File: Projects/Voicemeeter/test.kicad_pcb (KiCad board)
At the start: 2 copper layers, 348.5 x 271.7 mm, 226 parts, among them J501 CONN_01X05, J502 CONN_01X03, J503 CONN_01X05, J504 CONN_01X02, J505 CONN_01X03, J506 CONN_01X02, J509 Screw_Terminal_1x02, SW201 SW_SPDT_6pin, SW202 SW_SPDT_6pin, SW203 SW_SPDT_6pin, SW204 SW_SPDT_6pin, SW205 SW_SPDT_6pin, SW206 SW_SPDT_6pin, SW207 SW_SPDT_6pin, SW208 SW_SPDT_6pin, SW209 SW_SPDT_6pin, SW210 SW_SPDT_6pin, SW211 SW_SPDT_6pin, SW212 SW_SPDT_6pin, SW213 SW_SPDT_6pin, SW214 SW_SPDT_6pin, SW215 SW_SPDT_6pin, SW216 SW_SPDT_6pin, SW217 SW_SPDT_6pin, SW218 SW_SPDT_6pin, SW219 SW_SPDT_6pin, SW220 SW_SPDT_6pin, SW221 SW_SPDT_6pin, SW222 SW_SPDT_6pin, SW223 SW_SPDT_6pin, SW224 SW_SPDT_6pin, SW225 SW_SPDT_6pin, SW226 SW_SPDT_6pin, SW227 SW_SPDT_6pin, SW228 SW_SPDT_6pin, SW229 SW_SPDT_6pin, SW230 SW_SPDT_6pin, SW231 SW_SPDT_6pin, SW232 SW_SPDT_6pin, SW233 SW_SPDT_6pin, SW234 SW_SPDT_6pin, SW235 SW_SPDT_6pin, SW236 SW_SPDT_6pin, SW237 SW_SPDT_6pin, SW238 SW_SPDT_6pin, SW239 SW_SPDT_6pin, SW240 SW_SPDT_6pin, SW241 SW_SPDT_6pin, SW242 SW_SPDT_6pin, SW243 SW_SPDT_6pin, SW244 SW_SPDT_6pin, SW245 SW_SPDT_6pin, SW246 SW_SPDT_6pin, SW247 SW_SPDT_6pin, SW248 SW_SPDT_6pin, SW249 SW_SPDT_6pin, SW250 SW_SPDT_6pin, SW251 SW_SPDT_6pin, SW252 SW_SPDT_6pin, SW253 SW_SPDT_6pin, SW254 SW_SPDT_6pin, SW255 SW_SPDT_6pin, SW501 SW_Push, U401 74HC4051, U402 74HC4051, U403 74HC4051, U404 74HC4051, U405 74HC4051, U406 74HC4051, U407 74HC4051, U408 74HC4051, U409 74HC4051, U410 74HC4051, U501 stm32f103-china-MS, U502 PC817

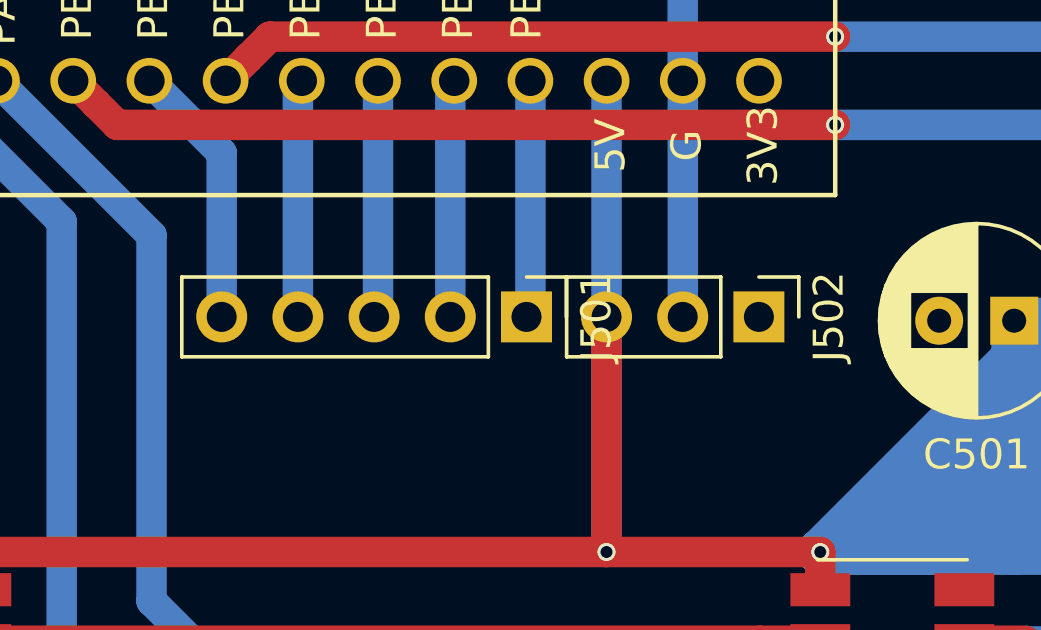
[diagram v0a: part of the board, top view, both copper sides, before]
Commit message: fixed a header
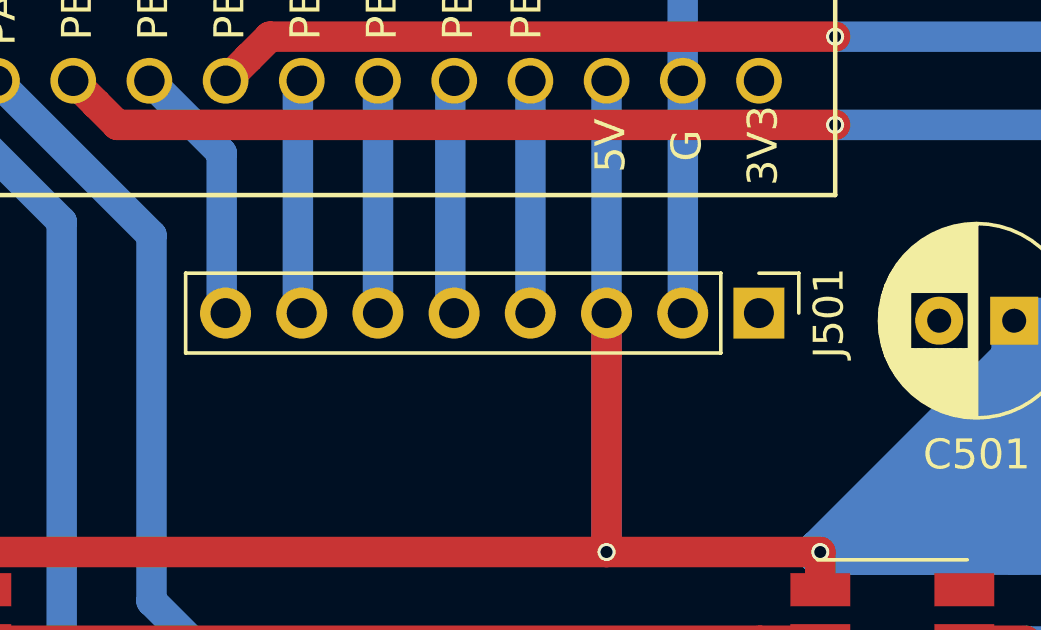
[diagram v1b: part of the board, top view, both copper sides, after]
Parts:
- removed J502: CONN_01X03, Pin_Headers:Pin_Header_Straight_1x03_Pitch2.54mm
- J501: value CONN_01X05 -> Conn_01x08; footprint Pin_Headers:Pin_Header_Straight_1x05_Pitch2.54mm -> Pin_Headers:Pin_Header_Straight_1x08_Pitch2.54mm
- moved J501 7.75 mm to (273.7, 108.0)
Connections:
- J501 pad 1: Net-(J501-Pad1) -> +3V3
- J501 pad 2: Net-(J501-Pad2) -> GND
- J501 pad 3: Net-(J501-Pad3) -> +5V
- U501 pad 12: Net-(J501-Pad5) -> Net-(J501-Pad8)
- U501 pad 14: Net-(J501-Pad4) -> Net-(J501-Pad7)
- U501 pad 15: Net-(J501-Pad3) -> Net-(J501-Pad6)
- U501 pad 16: Net-(J501-Pad2) -> Net-(J501-Pad5)
- U501 pad 17: Net-(J501-Pad1) -> Net-(J501-Pad4)
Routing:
- net Net-(J501-Pad8): track 0.00 -> 8.62 mm
- net Net-(J501-Pad7): track 0.00 -> 7.67 mm
- net Net-(J501-Pad3): track 7.67 -> 0.00 mm
- net Net-(J501-Pad2): track 7.67 -> 0.00 mm
- net Net-(J501-Pad1): track 7.67 -> 0.00 mm
- net Net-(J501-Pad6): track 0.00 -> 7.49 mm
- net Net-(J501-Pad5): track 8.62 -> 7.67 mm

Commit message: stuff
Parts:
- added C1, C10, C11, C12, C13, C14, C15, C16, C17, C18, C19, C2, C20, C21, C22, C3, C4, C5, C6, C7, C8, C9: 10uF, Capacitors_SMD:C_1206_HandSoldering, F.Cu at (206.8, 256.4)
- added C23, C24: 220uF, Capacitors_THT:CP_Radial_D6.3mm_P2.50mm, F.Cu at (206.8, 256.4)
- added D1: D, Diodes_THT:D_DO-41_SOD81_P12.70mm_Horizontal, F.Cu at (206.8, 256.4)
- added J1: SPARE, Pin_Headers:Pin_Header_Straight_1x05_Pitch2.54mm, F.Cu at (206.8, 256.4)
- added J2, J4: GS2, MATHSTERK:SB2, F.Cu at (206.8, 256.4)
- added J3: Screw_Terminal_01x02, Connectors_Terminal_Blocks:TerminalBlock_Altech_AK300-2_P5.00mm, F.Cu at (206.8, 256.4)
- added J5: MIDI OUT, Pin_Headers:Pin_Header_Straight_1x03_Pitch2.54mm, F.Cu at (206.8, 256.4)
- added J6: MIDI IN, Pin_Headers:Pin_Header_Straight_1x02_Pitch2.54mm, F.Cu at (206.8, 256.4)
- added LED1, LED10, LED11, LED12, LED13, LED14, LED15, LED16, LED17, LED18, LED19, LED2, LED20, LED21, LED22, LED23, LED24, LED25, LED26, LED27, LED28, LED29, LED3, LED30, LED31, LED32, LED4, LED5, LED6, LED7, LED8, LED9: SK9822, LEDs:LED_RGB_5050-6, F.Cu at (206.8, 256.4)
- added R1, R10, R11, R12, R13, R14, R15, R16, R17, R18, R19, R2, R20, R21, R22, R23, R24, R25, R26, R27, R28, R29, R3, R30, R31, R32, R33, R34, R35, R36, R37, R38, R39, R4, R40, R41, R42, R43, R44, R45, R46, R47, R48, R49, R5, R50, R51, R52, R53, R54, R55, R6, R7, R8, R9: 10K, Resistors_SMD:R_1206_HandSoldering, F.Cu at (206.8, 256.4)
- added R56, R57, R58, R59, R60, R61, R62, R63, R64, R65, R66, R67, R68, R70, R71, R72, R73, R75, R77: 10k, Resistors_SMD:R_1206_HandSoldering, F.Cu at (206.8, 256.4)
- added R69, R76: 220R, Resistors_SMD:R_1206_HandSoldering, F.Cu at (206.8, 256.4)
- added R74: 330R, Resistors_SMD:R_1206_HandSoldering, F.Cu at (206.8, 256.4)
- added RESET1: SW_Push, Buttons_Switches_THT:SW_PUSH-12mm, F.Cu at (206.8, 256.4)
- added RV1, RV11, RV12, RV13, RV15, RV16, RV17, RV3, RV4, RV6, RV7, RV9: POT, Potentiometers:Potentiometer_Omeg_PC16PU_Horizontal, F.Cu at (206.8, 256.4)
- added RV10, RV14, RV18, RV19, RV2, RV20, RV21, RV22, RV5, RV8: SLIDEPOT, MATHSTERK:slidepot, F.Cu at (206.8, 256.4)
- added SW1, SW10, SW11, SW12, SW13, SW14, SW15, SW16, SW17, SW18, SW19, SW2, SW20, SW21, SW22, SW23, SW24, SW25, SW26, SW27, SW28, SW29, SW3, SW30, SW31, SW32, SW33, SW34, SW35, SW36, SW37, SW38, SW39, SW4, SW40, SW41, SW42, SW43, SW44, SW45, SW46, SW47, SW48, SW49, SW5, SW50, SW51, SW52, SW53, SW54, SW55, SW6, SW7, SW8, SW9: SW_SPDT_6pin, MATHSTERK:8mm_push_button, F.Cu at (206.8, 256.4)
- added SW56: PEC11R-4215F-S0024, MATHSTERK:Rotary_Encoder_Switched_PEC11R, F.Cu at (206.8, 256.4)
- added U1, U10, U2, U3, U4, U5, U6, U7, U8, U9: 74HC4051, Housings_DIP:DIP-16_W7.62mm_LongPads, F.Cu at (206.8, 256.4)
- added U12: PC817, Housings_DIP:DIP-4_W7.62mm, F.Cu at (206.8, 256.4)

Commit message: WIP
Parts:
- removed C1, C10, C11, C12, C13, C14, C15, C16, C17, C18, C19, C2, C20, C21, C22, C3, C4, C5, C6, C7, C8, C9: 10uF, Capacitors_SMD:C_1206_HandSoldering
- removed C23, C24: 220uF, Capacitors_THT:CP_Radial_D6.3mm_P2.50mm
- removed D1: D, Diodes_THT:D_DO-41_SOD81_P12.70mm_Horizontal
- removed J1: SPARE, Pin_Headers:Pin_Header_Straight_1x05_Pitch2.54mm
- removed J2, J4: GS2, MATHSTERK:SB2
- removed J3: Screw_Terminal_01x02, Connectors_Terminal_Blocks:TerminalBlock_Altech_AK300-2_P5.00mm
- removed J5: MIDI OUT, Pin_Headers:Pin_Header_Straight_1x03_Pitch2.54mm
- removed J6: MIDI IN, Pin_Headers:Pin_Header_Straight_1x02_Pitch2.54mm
- removed LED1, LED10, LED11, LED12, LED13, LED14, LED15, LED16, LED17, LED18, LED19, LED2, LED20, LED21, LED22, LED23, LED24, LED25, LED26, LED27, LED28, LED29, LED3, LED30, LED31, LED32, LED4, LED5, LED6, LED7, LED8, LED9: SK9822, LEDs:LED_RGB_5050-6
- removed R1, R10, R11, R12, R13, R14, R15, R16, R17, R18, R19, R2, R20, R21, R22, R23, R24, R25, R26, R27, R28, R29, R3, R30, R31, R32, R33, R34, R35, R36, R37, R38, R39, R4, R40, R41, R42, R43, R44, R45, R46, R47, R48, R49, R5, R50, R51, R52, R53, R54, R55, R6, R7, R8, R9: 10K, Resistors_SMD:R_1206_HandSoldering
- removed R56, R57, R58, R59, R60, R61, R62, R63, R64, R65, R66, R67, R68, R70, R71, R72, R73, R75, R77: 10k, Resistors_SMD:R_1206_HandSoldering
- removed R69, R76: 220R, Resistors_SMD:R_1206_HandSoldering
- removed R74: 330R, Resistors_SMD:R_1206_HandSoldering
- removed RESET1: SW_Push, Buttons_Switches_THT:SW_PUSH-12mm
- removed RV1, RV11, RV12, RV13, RV15, RV16, RV17, RV3, RV4, RV6, RV7, RV9: POT, Potentiometers:Potentiometer_Omeg_PC16PU_Horizontal
- removed RV10, RV14, RV18, RV19, RV2, RV20, RV21, RV22, RV5, RV8: SLIDEPOT, MATHSTERK:slidepot
- removed SW1, SW10, SW11, SW12, SW13, SW14, SW15, SW16, SW17, SW18, SW19, SW2, SW20, SW21, SW22, SW23, SW24, SW25, SW26, SW27, SW28, SW29, SW3, SW30, SW31, SW32, SW33, SW34, SW35, SW36, SW37, SW38, SW39, SW4, SW40, SW41, SW42, SW43, SW44, SW45, SW46, SW47, SW48, SW49, SW5, SW50, SW51, SW52, SW53, SW54, SW55, SW6, SW7, SW8, SW9: SW_SPDT_6pin, MATHSTERK:8mm_push_button
- removed SW56: PEC11R-4215F-S0024, MATHSTERK:Rotary_Encoder_Switched_PEC11R
- removed U1, U10, U2, U3, U4, U5, U6, U7, U8, U9: 74HC4051, Housings_DIP:DIP-16_W7.62mm_LongPads
- removed U12: PC817, Housings_DIP:DIP-4_W7.62mm
- added J502: GS2, MATHSTERK:SB2, F.Cu at (306.6, 93.3)
- added R504: 10k, Resistors_SMD:R_1206_HandSoldering, F.Cu at (328.2, 88.3)
- added R505: 10k, Resistors_SMD:R_1206_HandSoldering, F.Cu at (325.4, 70.9)
- added R506: 10k, Resistors_SMD:R_1206_HandSoldering, F.Cu at (300.4, 92.1)
- added R507: 10k, Resistors_SMD:R_1206_HandSoldering, F.Cu at (318.5, 70.9)
- added R508: 10k, Resistors_SMD:R_1206_HandSoldering, F.Cu at (304.6, 82.5)
- added R509: 10k, Resistors_SMD:R_1206_HandSoldering, F.Cu at (311.5, 76.7)
- added R510: 10k, Resistors_SMD:R_1206_HandSoldering, F.Cu at (293.4, 92.1)
- added R511: 10k, Resistors_SMD:R_1206_HandSoldering, F.Cu at (304.6, 76.7)
- added R512: 10k, Resistors_SMD:R_1206_HandSoldering, F.Cu at (311.5, 70.9)
- added R513: 10k, Resistors_SMD:R_1206_HandSoldering, F.Cu at (304.6, 70.9)
- added R514: 220R, Resistors_SMD:R_1206_HandSoldering, F.Cu at (318.5, 76.7)
- added R515: 10k, Resistors_SMD:R_1206_HandSoldering, F.Cu at (311.5, 82.5)
- added R516: 10k, Resistors_SMD:R_1206_HandSoldering, F.Cu at (286.5, 92.1)
- added R517: 10k, Resistors_SMD:R_1206_HandSoldering, F.Cu at (307.3, 88.3)
- added R518: 10k, Resistors_SMD:R_1206_HandSoldering, F.Cu at (318.5, 82.5)
- added R519: 330R, Resistors_SMD:R_1206_HandSoldering, F.Cu at (325.4, 76.7)
- added R520: 10k, Resistors_SMD:R_1206_HandSoldering, F.Cu at (314.3, 88.3)
- added R521: 220R, Resistors_SMD:R_1206_HandSoldering, F.Cu at (325.4, 82.5)
- added R522: 10k, Resistors_SMD:R_1206_HandSoldering, F.Cu at (321.2, 88.3)
- added RESET501: SW_Push, Buttons_Switches_THT:SW_PUSH-12mm, F.Cu at (215.3, 84.9)
- J501: value Conn_01x08 -> SPARE
- J503: value CONN_01X05 -> Screw_Terminal_01x02
- J504: value CONN_01X02 -> GS2
- J505: value CONN_01X03 -> MIDI OUT
- J506: value CONN_01X02 -> MIDI IN
- R501, R503: value 220R -> 10k
- R502: value 330R -> 10k
- SW501: value SW_Push -> PEC11R-4215F-S0024; footprint Buttons_Switches_THT:SW_PUSH-12mm -> MATHSTERK:Rotary_Encoder_Switched_PEC11R
- moved LED618 435.7 mm to (439.2, 5.70)
- moved LED617 431.8 mm to (408.2, -3.15)
- moved LED619 411.5 mm to (431.4, 5.70)
- moved LED620 405.7 mm to (439.2, -3.15)
- moved LED621 371.2 mm to (423.7, 5.70)
- moved LED615 369.8 mm to (423.7, -20.8), turned to 0 degrees
- moved LED622 366.5 mm to (431.4, -3.15)
- moved LED616 364.5 mm to (384.9, -20.8), turned to 0 degrees
- moved LED623 362.5 mm to (439.2, -12.0)
- moved LED624 353.6 mm to (439.2, -20.8)
- moved LED614 328.8 mm to (415.9, -12.0), turned to 0 degrees
- moved LED610 302.8 mm to (415.9, -20.8), turned to 0 degrees
- moved LED611 297.2 mm to (408.2, -12.0), turned to 0 degrees
- moved LED612 278.9 mm to (400.4, -3.15), turned to 0 degrees
- moved LED609 268.3 mm to (408.2, -20.8), turned to 0 degrees
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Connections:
- C301 pad 2: /Mux/HA11 -> /Capacitors/HA11
- C302 pad 2: /Mux/HA12 -> /Capacitors/HA12
- C303 pad 2: /Mux/HA13 -> /Capacitors/HA13
- C304 pad 2: /Mux/HA21 -> /Capacitors/HA21
- C305 pad 2: /Mux/HA22 -> /Capacitors/HA22
- C306 pad 2: /Mux/HA23 -> /Capacitors/HA23
- C307 pad 2: /Mux/HA31 -> /Capacitors/HA31
- C308 pad 2: /Mux/HA32 -> /Capacitors/HA32
- C309 pad 2: /Mux/HA33 -> /Capacitors/HA33
- C310 pad 2: /Mux/DA11 -> /Capacitors/DA11
- C311 pad 2: /Mux/DA12 -> /Capacitors/DA12
- C312 pad 2: /Mux/DA13 -> /Capacitors/DA13
- C313 pad 2: /Mux/DA14 -> /Capacitors/DA14
- C314 pad 2: /Mux/DA21 -> /Capacitors/DA21
- C315 pad 2: /Mux/DA22 -> /Capacitors/DA22
- C316 pad 2: /Mux/DA23 -> /Capacitors/DA23
- C317 pad 2: /Mux/DA24 -> /Capacitors/DA24
- C318 pad 2: /Mux/OA1 -> /Capacitors/OA1
- C319 pad 2: /Mux/OA2 -> /Capacitors/OA2
- C320 pad 2: /Mux/OA3 -> /Capacitors/OA3
- C321 pad 2: /Mux/OA4 -> /Capacitors/OA4
- C322 pad 2: /Mux/OA5 -> /Capacitors/OA5
- J501 pad 6: Net-(J501-Pad6) -> (no net)
- J501 pad 7: Net-(J501-Pad7) -> (no net)
- J501 pad 8: Net-(J501-Pad8) -> (no net)
- J503 pad 1: Net-(J503-Pad1) -> +5V
- J503 pad 2: Net-(J503-Pad2) -> GND
- J503 pad 3: Net-(J503-Pad3) -> (no net)
- J503 pad 4: Net-(J503-Pad4) -> (no net)
- J503 pad 5: Net-(J503-Pad5) -> (no net)
- LED601 pad 1: /LED Driver/SK2 -> /LEDs/SK2
- LED601 pad 2: /LED Driver/SK1 -> /LEDs/SK1
- R501 pad 1: Net-(J505-Pad3) -> Net-(R501-Pad1)
- R501 pad 2: Net-(R501-Pad2) -> /Mux/M25
- R502 pad 1: +3V3 -> Net-(R502-Pad1)
- R502 pad 2: Net-(R502-Pad2) -> /Mux/M26
- R503 pad 1: Net-(J505-Pad1) -> Net-(R503-Pad1)
- R503 pad 2: +3V3 -> /Mux/M27
- RV201 pad 2: /Mux/HA12 -> /Capacitors/HA12
- RV202 pad 2: /Mux/HA11 -> /Capacitors/HA11
- RV203 pad 2: /Mux/HA13 -> /Capacitors/HA13
- RV204 pad 2: /Mux/HA22 -> /Capacitors/HA22
- RV205 pad 2: /Mux/HA21 -> /Capacitors/HA21
- RV206 pad 2: /Mux/HA23 -> /Capacitors/HA23
- RV207 pad 2: /Mux/HA32 -> /Capacitors/HA32
- RV208 pad 2: /Mux/HA31 -> /Capacitors/HA31
- RV209 pad 2: /Mux/HA33 -> /Capacitors/HA33
- RV210 pad 2: /Mux/DA11 -> /Capacitors/DA11
- RV211 pad 2: /Mux/DA12 -> /Capacitors/DA12
- RV212 pad 2: /Mux/DA14 -> /Capacitors/DA14
- RV213 pad 2: /Mux/DA13 -> /Capacitors/DA13
- RV214 pad 2: /Mux/DA21 -> /Capacitors/DA21
- RV215 pad 2: /Mux/DA22 -> /Capacitors/DA22
- RV216 pad 2: /Mux/DA24 -> /Capacitors/DA24
- RV217 pad 2: /Mux/DA23 -> /Capacitors/DA23
- RV218 pad 2: /Mux/OA1 -> /Capacitors/OA1
- RV219 pad 2: /Mux/OA2 -> /Capacitors/OA2
- RV220 pad 2: /Mux/OA3 -> /Capacitors/OA3
- RV221 pad 2: /Mux/OA4 -> /Capacitors/OA4
- RV222 pad 2: /Mux/OA5 -> /Capacitors/OA5
- SW501 pad 1: GND -> Net-(R515-Pad1)
- SW501 pad 2: Net-(SW501-Pad2) -> +3V3
- U401 pad 1: /Mux/HA13 -> /Capacitors/HA13
- U401 pad 12: /Mux/HA32 -> /Capacitors/HA32
- U401 pad 13: /Mux/HA31 -> /Capacitors/HA31
- U401 pad 14: /Mux/HA23 -> /Capacitors/HA23
- U401 pad 15: /Mux/HA11 -> /Capacitors/HA11
- U401 pad 2: /Mux/HA12 -> /Capacitors/HA12
- U401 pad 4: /Mux/HA21 -> /Capacitors/HA21
- U401 pad 5: /Mux/HA22 -> /Capacitors/HA22
- U402 pad 12: /Mux/OA2 -> /Capacitors/OA2
- U402 pad 13: /Mux/OA3 -> /Capacitors/OA3
- U402 pad 14: /Mux/OA4 -> /Capacitors/OA4
- U402 pad 15: /Mux/OA5 -> /Capacitors/OA5
- U402 pad 2: /Mux/DA21 -> /Capacitors/DA21
- U402 pad 4: /Mux/DA11 -> /Capacitors/DA11
- U402 pad 5: /Mux/OA1 -> /Capacitors/OA1
- U403 pad 1: /Mux/DA23 -> /Capacitors/DA23
- U403 pad 12: /Mux/DA12 -> /Capacitors/DA12
- U403 pad 13: /Mux/DA13 -> /Capacitors/DA13
- U403 pad 14: /Mux/DA14 -> /Capacitors/DA14
- U403 pad 15: /Mux/DA22 -> /Capacitors/DA22
- U403 pad 2: /Mux/DA24 -> /Capacitors/DA24
- U403 pad 5: /Mux/HA33 -> /Capacitors/HA33
- U501 pad 1: /Mux/M1 -> Net-(J504-Pad2)
- U501 pad 10: /Mux/M27 -> Net-(R510-Pad1)
- U501 pad 11: /LED Driver/SK1 -> /LEDs/SK1
- U501 pad 12: Net-(J501-Pad8) -> Net-(J501-Pad5)
- U501 pad 13: /LED Driver/SK2 -> /LEDs/SK2
- U501 pad 14: Net-(J501-Pad7) -> Net-(R501-Pad1)
- U501 pad 15: Net-(J501-Pad6) -> Net-(R502-Pad1)
- U501 pad 16: Net-(J501-Pad5) -> Net-(R503-Pad1)
- U501 pad 17: Net-(J501-Pad4) -> /STM/OLED4
- U501 pad 2: /Mux/M2 -> /STM/OLED1
- U501 pad 25: Net-(J504-Pad2) -> Net-(J502-Pad2)
- U501 pad 26: Net-(J504-Pad1) -> /STM/ROT3
- U501 pad 27: Net-(R502-Pad2) -> Net-(R519-Pad2)
- U501 pad 28: Net-(R501-Pad2) -> Net-(R514-Pad2)
- U501 pad 29: /Mux/M11 -> Net-(R513-Pad2)
- U501 pad 3: /Mux/M3 -> /STM/OLED2
- U501 pad 30: /Mux/M12 -> Net-(R512-Pad2)
- U501 pad 31: /Mux/M13 -> Net-(R511-Pad2)
- U501 pad 32: Net-(J503-Pad5) -> /STM/ROT2
- U501 pad 33: Net-(J503-Pad4) -> /STM/ROT1
- U501 pad 34: Net-(J503-Pad3) -> /STM/OLED7
- U501 pad 35: Net-(J503-Pad2) -> /STM/OLED6
- U501 pad 36: Net-(J503-Pad1) -> /STM/OLED5
- U501 pad 37: Net-(SW501-Pad2) -> Net-(RESET501-Pad2)
- U501 pad 4: /Mux/M21 -> /STM/OLED3
- U501 pad 5: /Mux/M22 -> Net-(R505-Pad1)
- U501 pad 6: /Mux/M23 -> Net-(R506-Pad1)
- U501 pad 7: /Mux/M24 -> Net-(R507-Pad1)
- U501 pad 8: /Mux/M25 -> Net-(R508-Pad1)
- U501 pad 9: /Mux/M26 -> Net-(R509-Pad1)
- U502 pad 4: Net-(R502-Pad2) -> Net-(R519-Pad2)
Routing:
- net /Mux/M1: track 666.8 -> 434.4 mm, vias 1 -> 0
- net Net-(J504-Pad2): track 13.8 -> 246.3 mm, vias 0 -> 1
- net /Mux/HA31: track 183.1 -> 0.00 mm, vias 4 -> 0
- net /Capacitors/HA31: track 0.00 -> 183.1 mm, vias 0 -> 4
- net Net-(R505-Pad1): track 0.00 -> 169.9 mm, vias 0 -> 4
- net /Mux/M22: track 202.9 -> 33.0 mm, vias 5 -> 1
- net /Mux/HA11: track 162.8 -> 0.00 mm
- net /Capacitors/HA11: track 0.00 -> 162.8 mm
- net /STM/OLED3: track 0.00 -> 155.5 mm, vias 0 -> 4
- net /Mux/M21: track 243.8 -> 88.3 mm, vias 7 -> 3
- net /Mux/OA5: track 144.6 -> 0.00 mm, vias 2 -> 0
- net /Capacitors/OA5: track 0.00 -> 144.6 mm, vias 0 -> 2
- net /Mux/HA21: track 141.7 -> 0.00 mm, vias 3 -> 0
- net /Capacitors/HA21: track 0.00 -> 141.7 mm, vias 0 -> 3
- net /Mux/DA24: track 123.7 -> 0.00 mm, vias 1 -> 0
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
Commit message: Zzzzz
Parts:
- moved LED618 433.0 mm to (68.4, 229.4)
- moved LED617 429.8 mm to (47.1, 229.9)
- moved LED619 410.6 mm to (87.7, 230.5)
- moved LED620 405.2 mm to (108.1, 230.5)
- moved LED621 369.1 mm to (129.4, 228.4)
- moved LED622 364.9 mm to (150.7, 229.9)
- moved LED623 361.2 mm to (170.0, 228.9)
- moved LED616 360.7 mm to (52.7, 119.7)
- moved LED624 351.1 mm to (192.4, 228.9)
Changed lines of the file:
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@@
   )
   (module LEDs:LED_RGB_5050-6 (layer F.Cu)
-    (at 384.925002 -20.848001)
+    (at 52.692 119.712)
     (descr http://cdn.sparkfun.com/datasheets/Components/LED/5060BRG4.pdf)
     (tags "RGB LED 5050-6")
@@
   )
   (module LEDs:LED_RGB_5050-6 (layer F.Cu)
-    (at 408.175002 -3.148001)
+    (at 47.104 229.948)
     (descr http://cdn.sparkfun.com/datasheets/Components/LED/5060BRG4.pdf)
     (tags "RGB LED 5050-6")
@@
   )
   (module LEDs:LED_RGB_5050-6 (layer F.Cu)
-    (at 439.175002 5.701999)
+    (at 68.44 229.44)
     (descr http://cdn.sparkfun.com/datasheets/Components/LED/5060BRG4.pdf)
     (tags "RGB LED 5050-6")
@@
   )
   (module LEDs:LED_RGB_5050-6 (layer F.Cu)
-    (at 431.425002 5.701999)
+    (at 87.744 230.456)
     (descr http://cdn.sparkfun.com/datasheets/Components/LED/5060BRG4.pdf)
     (tags "RGB LED 5050-6")
@@
   )
   (module LEDs:LED_RGB_5050-6 (layer F.Cu)
-    (at 439.175002 -3.148001)
+    (at 108.064 230.456)
     (descr http://cdn.sparkfun.com/datasheets/Components/LED/5060BRG4.pdf)
     (tags "RGB LED 5050-6")
@@
   )
   (module LEDs:LED_RGB_5050-6 (layer F.Cu)
-    (at 423.675002 5.701999)
+    (at 129.4 228.424)
     (descr http://cdn.sparkfun.com/datasheets/Components/LED/5060BRG4.pdf)
     (tags "RGB LED 5050-6")
@@
   )
   (module LEDs:LED_RGB_5050-6 (layer F.Cu)
-    (at 431.425002 -3.148001)
+    (at 150.736 229.948)
     (descr http://cdn.sparkfun.com/datasheets/Components/LED/5060BRG4.pdf)
     (tags "RGB LED 5050-6")
@@
   )
   (module LEDs:LED_RGB_5050-6 (layer F.Cu)
-    (at 439.175002 -11.998001)
+    (at 170.04 228.932)
     (descr http://cdn.sparkfun.com/datasheets/Components/LED/5060BRG4.pdf)
     (tags "RGB LED 5050-6")
@@
   )
   (module LEDs:LED_RGB_5050-6 (layer F.Cu)
-    (at 439.175002 -20.848001)
-    (descr http://cdn.sparkfun.com/datasheets/Components/LED/5060BRG4.pdf)
-    (tags "RGB LED 5050-6")
+    (at 192.392 228.932)
+    (descr http://cdn.sparkfun.com/datasheets/Components/LED/5060BRG4.pdf)
+    (tags "RGB LED 5050-6")

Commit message: switching to desktop
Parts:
- moved LED615 369.8 mm to (81.3, 118.9), turned to 180 degrees
- moved LED614 328.8 mm to (114.3, 118.9), turned to 180 degrees
- moved LED610 302.8 mm to (147.3, 118.9), turned to 180 degrees
- moved LED611 297.2 mm to (134.6, 104.1), turned to 90 degrees
- moved LED612 278.9 mm to (134.6, 81.3), turned to 90 degrees
- moved LED609 268.3 mm to (179.1, 118.9), turned to 180 degrees
- moved LED613 263.4 mm to (134.6, 58.4), turned to 90 degrees
- moved LED607 223.5 mm to (197.4, 81.3), turned to 90 degrees
- moved LED606 211.8 mm to (197.3, 104.0), turned to 90 degrees
- moved LED608 204.8 mm to (197.4, 58.4), turned to 90 degrees
- moved LED616 4.51 mm to (48.3, 118.9), turned to 180 degrees
- moved LED621 3.65 mm to (129.5, 232.1)
- moved LED623 3.34 mm to (171.2, 232.1)
- moved LED624 3.17 mm to (192.0, 232.1)
- moved LED618 3.04 mm to (66.9, 232.1)
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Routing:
- net Net-(J504-Pad2): track 246.3 -> 98.9 mm
- net /Mux/M1: track 434.4 -> 581.8 mm
- net Net-(LED616-Pad5): track 0.00 -> 120.8 mm, vias 0 -> 2
- net Net-(LED616-Pad6): track 0.00 -> 114.1 mm, vias 0 -> 2
- net Net-(LED613-Pad5): track 0.00 -> 77.3 mm, vias 0 -> 2
- net Net-(LED613-Pad6): track 0.00 -> 74.5 mm, vias 0 -> 2
- net Net-(LED608-Pad5): track 0.00 -> 71.8 mm, vias 0 -> 2
- net Net-(LED608-Pad6): track 0.00 -> 71.6 mm
- net Net-(LED609-Pad6): track 0.00 -> 30.0 mm
- net Net-(LED615-Pad6): track 0.00 -> 29.9 mm
- net Net-(LED614-Pad6): track 0.00 -> 29.9 mm
- net Net-(LED615-Pad5): track 0.00 -> 29.5 mm
- net Net-(LED614-Pad5): track 0.00 -> 29.5 mm
- net Net-(LED604-Pad6): track 0.00 -> 28.2 mm
- net Net-(LED604-Pad5): track 0.00 -> 28.2 mm
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
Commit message: uuuuuugh
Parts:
- removed C301, C302, C303, C304, C305, C306, C307, C308, C309, C310, C311, C312, C313, C314, C315, C316, C317, C318, C319, C320, C321, C322: 10uF, Capacitors_SMD:C_1206_HandSoldering
- removed J509: Screw_Terminal_1x02, TerminalBlock:TerminalBlock_bornier-2_P5.08mm
- removed LED601, LED602, LED603, LED604, LED605, LED606, LED607, LED608, LED609, LED610, LED611, LED612, LED613, LED614, LED615, LED616, LED617, LED618, LED619, LED620, LED621, LED622, LED623, LED624, LED625, LED626, LED627, LED628, LED629, LED630, LED631, LED632: SK9822, LEDs:LED_RGB_5050-6
- removed R201, R202, R203, R204, R205, R206, R207, R208, R209, R210, R211, R212, R213, R214, R215, R216, R217, R218, R219, R220, R221, R222, R223, R224, R225, R226, R227, R228, R229, R230, R231, R232, R233, R234, R235, R236, R237, R238, R239, R240, R241, R242, R243, R244, R245, R246, R247, R248, R249, R250, R251, R252, R253, R254, R255: 10K, Resistors_SMD:R_1206_HandSoldering
- removed REF** (x14): via_single, myelin-kicad:via_single
- removed RV201, RV203, RV204, RV206, RV207, RV209, RV211, RV212, RV213, RV215, RV216, RV217: POT, Potentiometers:Potentiometer_Omeg_PC16PU_Horizontal
- removed RV202, RV205, RV208, RV210, RV214, RV218, RV219, RV220, RV221, RV222: SLIDEPOT, pots:slidepot
- removed SW201, SW202, SW203, SW204, SW205, SW206, SW207, SW208, SW209, SW210, SW211, SW212, SW213, SW214, SW215, SW216, SW217, SW218, SW219, SW220, SW221, SW222, SW223, SW224, SW225, SW226, SW227, SW228, SW229, SW230, SW231, SW232, SW233, SW234, SW235, SW236, SW237, SW238, SW239, SW240, SW241, SW242, SW243, SW244, SW245, SW246, SW247, SW248, SW249, SW250, SW251, SW252, SW253, SW254, SW255: SW_SPDT_6pin, switches:8mm_push_button
- removed U501: stm32f103-china-MS, myelin-kicad:stm32f103c8t6-module-china-MS
- added OLED501: 1.5, MATHSTERK:OLED, F.Cu at (307.5, 35.0)
- J501: footprint Pin_Headers:Pin_Header_Straight_1x08_Pitch2.54mm -> Pin_Headers:Pin_Header_Straight_1x05_Pitch2.54mm
- J503: value Screw_Terminal_01x02 -> GS2; footprint Pin_Headers:Pin_Header_Straight_1x05_Pitch2.54mm -> Connectors_Terminal_Blocks:TerminalBlock_Altech_AK300-2_P5.00mm
- J504: footprint Pin_Headers:Pin_Header_Straight_1x02_Pitch2.54mm -> MATHSTERK:SB2
- R501, R502, R503, R504, R505, R506, R507, R508, R509, R510, R511, R512, R513, R515, R516, R517, R518, R520, R522: value 10k -> 10K
- moved U402 116.1 mm to (140.0, 68.4)
- moved C501 105.7 mm to (305.0, 5.00)
- moved J503 85.6 mm to (290.0, 5.00)
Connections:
- J503 pad 1: +5V -> Net-(J503-Pad1)
- J503 pad 2: GND -> Net-(J501-Pad5)
- R518 pad 1: GND -> Net-(R515-Pad1)
- R518 pad 2: Net-(R515-Pad1) -> GND
- R519 pad 1: +3V3 -> Net-(R519-Pad1)
- R519 pad 2: Net-(R519-Pad2) -> +3V3
- R520 pad 1: GND -> Net-(R516-Pad1)
- R520 pad 2: Net-(R516-Pad1) -> GND
- R522 pad 1: GND -> Net-(R517-Pad1)
- R522 pad 2: Net-(R517-Pad1) -> GND
- U401 pad 6: Net-(U401-Pad6) -> (no net)
- U401 pad 7: Net-(U401-Pad7) -> (no net)
- U402 pad 1: Net-(U402-Pad1) -> (no net)
- U402 pad 6: Net-(U402-Pad6) -> (no net)
- U402 pad 7: Net-(U402-Pad7) -> (no net)
- U403 pad 4: Net-(U403-Pad4) -> (no net)
- U403 pad 6: Net-(U403-Pad6) -> (no net)
- U403 pad 7: Net-(U403-Pad7) -> (no net)
- U404 pad 6: Net-(U404-Pad6) -> (no net)
- U404 pad 7: Net-(U404-Pad7) -> (no net)
- U405 pad 6: Net-(U405-Pad6) -> (no net)
- U405 pad 7: Net-(U405-Pad7) -> (no net)
- U406 pad 6: Net-(U406-Pad6) -> (no net)
- U406 pad 7: Net-(U406-Pad7) -> (no net)
- U407 pad 6: Net-(U407-Pad6) -> (no net)
- U407 pad 7: Net-(U407-Pad7) -> (no net)
- U408 pad 6: Net-(U408-Pad6) -> (no net)
- U408 pad 7: Net-(U408-Pad7) -> (no net)
- U409 pad 6: Net-(U409-Pad6) -> (no net)
- U409 pad 7: Net-(U409-Pad7) -> (no net)
- U410 pad 12: Net-(U410-Pad12) -> (no net)
- U410 pad 6: Net-(U410-Pad6) -> (no net)
- U410 pad 7: Net-(U410-Pad7) -> (no net)
- U502 pad 1: Net-(D501-Pad1) -> Net-(R519-Pad1)
- U502 pad 2: Net-(D501-Pad2) -> GND
- U502 pad 3: GND -> Net-(D501-Pad2)
- U502 pad 4: Net-(R519-Pad2) -> Net-(D501-Pad1)
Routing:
- net +5V: track 1179.4 -> 0.00 mm, vias 27 -> 0
- net /Mux/M2: track 659.9 -> 0.00 mm, vias 3 -> 0
- net /Mux/M1: track 581.8 -> 0.00 mm
- net /Mux/M3: track 576.3 -> 0.00 mm, vias 2 -> 0
- net /Mux/M11: track 183.7 -> 0.00 mm, vias 4 -> 0
- net /Capacitors/HA31: track 183.1 -> 0.00 mm, vias 4 -> 0
- net Net-(R505-Pad1): track 169.9 -> 0.00 mm, vias 4 -> 0
- net /Capacitors/HA11: track 162.8 -> 0.00 mm
- net /STM/OLED3: track 155.5 -> 0.00 mm, vias 4 -> 0
- net /Mux/HD21: track 149.4 -> 0.00 mm, vias 2 -> 0
- net /Capacitors/OA5: track 144.6 -> 0.00 mm, vias 2 -> 0
- net /Capacitors/HA21: track 141.7 -> 0.00 mm, vias 3 -> 0
- net /Mux/HD22: track 138.6 -> 0.00 mm, vias 2 -> 0
- net /Mux/HD31: track 130.1 -> 0.00 mm, vias 1 -> 0
- net /Mux/HD11: track 129.5 -> 0.00 mm
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- removed copper zone on B.Cu, net +3V3
- removed copper zone on F.Cu, net GND
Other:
- board size 348.5 x 271.7 mm -> 678.5 x 302.5 mm
